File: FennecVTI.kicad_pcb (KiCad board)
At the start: 2 copper layers, 218 x 131.9 mm, 89 parts, among them J1 Expansion Connector, J2 Slot Select, J3 Conn_Coaxial, J4 MDA/CGA connector, J5 DB15_Female, J6 DIP14 Keyboard Connector, J7 User Connector, Q1 2N3906, U1 74LS191, U10 74LS574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

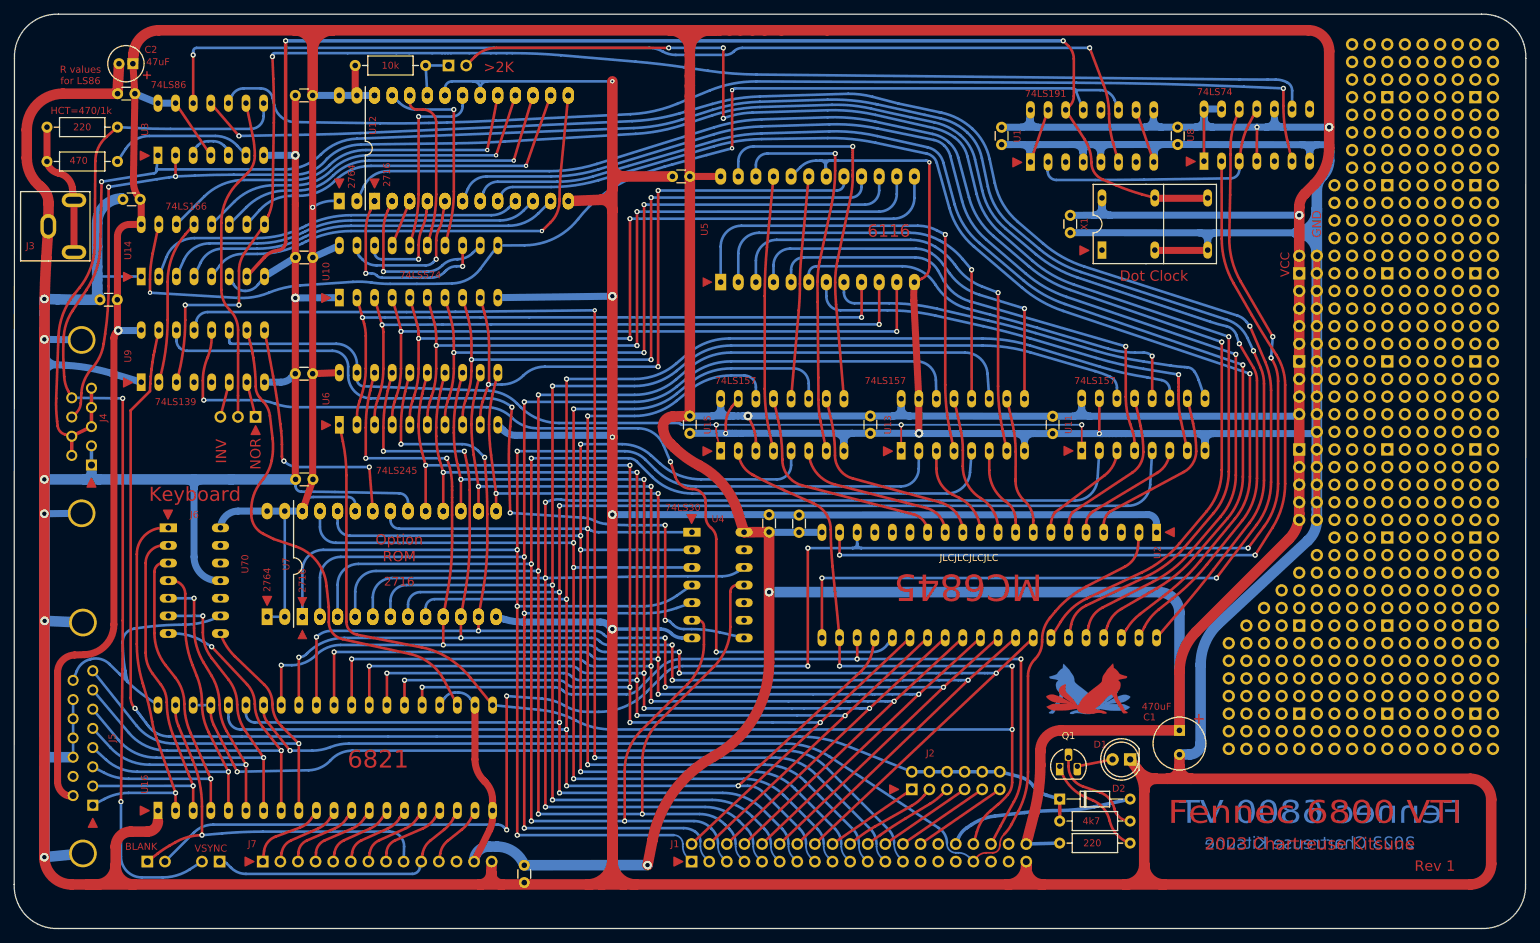
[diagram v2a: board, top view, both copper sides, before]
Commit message: Tweaked 2764 pinouts, cleanup DRC
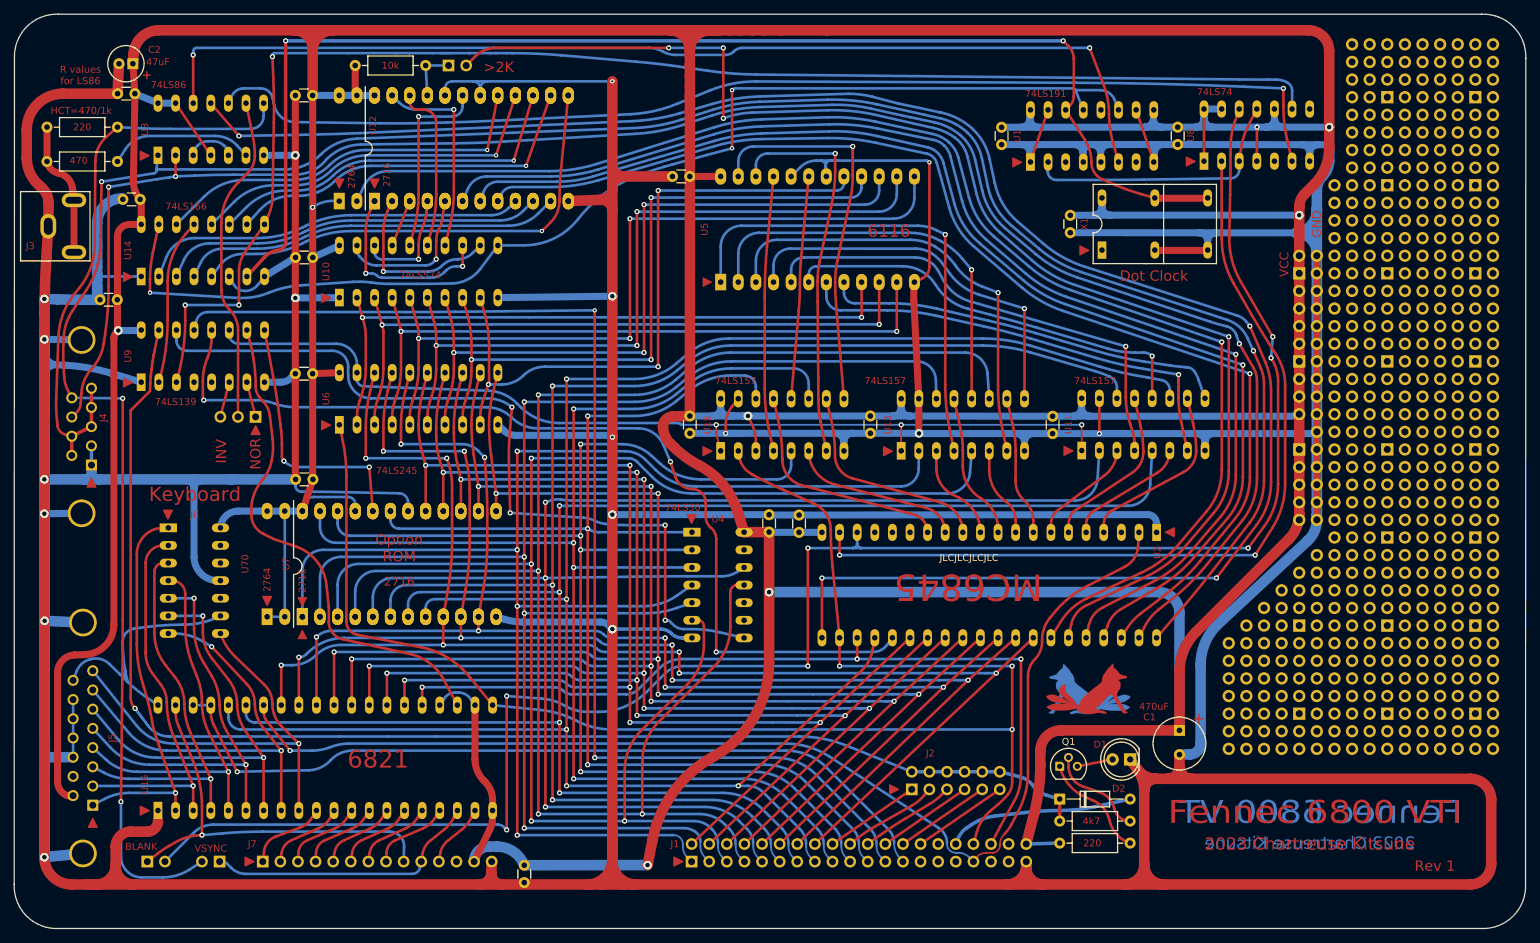
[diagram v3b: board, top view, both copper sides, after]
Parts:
- Q1: footprint Package_TO_SOT_THT:TO-92_HandSolder -> Package_TO_SOT_THT:TO-92
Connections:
- J4 pad 0: (no net) -> GND
- J5 pad 0: (no net) -> GND
- U120 pad 1: unconnected-(U120-VPP-Pad1) -> VCC
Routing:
- net /~{VRAMCS}: track 141.7 -> 141.2 mm
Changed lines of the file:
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@@
   (net 157 "unconnected-(U9A-O1-Pad5)")
   (net 158 "unconnected-(X1-NC-Pad1)")
-  (net 159 "unconnected-(U120-VPP-Pad1)")
   (footprint "Connector_PinHeader_2.54mm:PinHeader_1x14_P2.54mm_Vertical" (layer "F.Cu")
     (at 72.771 147.828 90)
@@
     (fp_arc (start 5.36 1.42) (mid 6.96 -0.18) (end 8.56 1.42)
       (stroke (width 0.1) (type solid)) (layer "F.Fab"))
-    (pad "0" thru_hole circle (at -18.04 1.42 270) (size 4 4) (drill 3.2) (layers "*.Cu" "*.Mask"))
-    (pad "0" thru_hole circle (at 6.96 1.42 270) (size 4 4) (drill 3.2) (layers "*.Cu" "*.Mask"))
+    (pad "0" thru_hole circle (at -18.04 1.42 270) (size 4 4) (drill 3.2) (layers "*.Cu" "*.Mask")
+      (net 2 "GND"))
+    (pad "0" thru_hole circle (at 6.96 1.42 270) (size 4 4) (drill 3.2) (layers "*.Cu" "*.Mask")
+      (net 2 "GND"))
     (pad "1" thru_hole rect (at 0 0 270) (size 1.6 1.6) (drill 1) (layers "*.Cu" "*.Mask")
       (net 2 "GND") (pinfunction "1") (pintype "passive"))
@@
     )
   )
-  (footprint "Package_TO_SOT_THT:TO-92_HandSolder" (layer "F.Cu")
+  (footprint "Package_TO_SOT_THT:TO-92" (layer "F.Cu")
     (at 187.706 134.091)
-    (descr "TO-92 leads molded, narrow, drill 0.75mm, handsoldering variant with enlarged pads (see NXP sot054_po.pdf)")
+    (descr "TO-92 leads molded, narrow, drill 0.75mm (see NXP sot054_po.pdf)")
     (tags "to-92 sc-43 sc-43a sot54 PA33 transistor")
     (property "Sheetfile" "FennecVTI.kicad_sch")
@@
     (property "ki_keywords" "PNP Transistor")
     (attr through_hole)
-    (fp_text reference "Q1" (at 1.27 -4.4) (layer "F.SilkS")
+    (fp_text reference "Q1" (at 1.27 -3.56) (layer "F.SilkS")
         (effects (font (size 1 1) (thickness 0.15)))
     )
@@
     (fp_line (start -0.53 1.85) (end 3.07 1.85)
       (stroke (width 0.12) (type solid)) (layer "F.SilkS"))
-    (fp_arc (start -0.541875 1.841741) (mid -1.247231 -0.581764) (end 0.45 -2.45)
+    (fp_arc (start -0.568478 1.838478) (mid -1.132087 -0.994977) (end 1.27 -2.6)
       (stroke (width 0.12) (type solid)) (layer "F.SilkS"))
-    (fp_arc (start 2.05 -2.45) (mid 3.769931 -0.601036) (end 3.078445 1.827684)
+    (fp_arc (start 1.27 -2.6) (mid 3.672087 -0.994977) (end 3.108478 1.838478)
       (stroke (width 0.12) (type solid)) (layer "F.SilkS"))
-    (fp_line (start -1.46 -3.05) (end -1.46 2.01)
+    (fp_line (start -1.46 -2.73) (end -1.46 2.01)
       (stroke (width 0.05) (type solid)) (layer "F.CrtYd"))
-    (fp_line (start -1.46 -3.05) (end 4 -3.05)
+    (fp_line (start -1.46 -2.73) (end 4 -2.73)
       (stroke (width 0.05) (type solid)) (layer "F.CrtYd"))
     (fp_line (start 4 2.01) (end -1.46 2.01)
       (stroke (width 0.05) (type solid)) (layer "F.CrtYd"))
-    (fp_line (start 4 2.01) (end 4 -3.05)
+    (fp_line (start 4 2.01) (end 4 -2.73)
       (stroke (width 0.05) (type solid)) (layer "F.CrtYd"))
     (fp_line (start -0.5 1.75) (end 3 1.75)
@@
     (fp_arc (start 1.27 -2.48) (mid 3.561221 -0.949055) (end 3.023625 1.753625)
       (stroke (width 0.1) (type solid)) (layer "F.Fab"))
-    (pad "1" thru_hole rect (at 0 0) (size 1.1 1.8) (drill 0.75 (offset 0 0.4)) (layers "*.Cu" "*.Mask")
+    (pad "1" thru_hole roundrect (at 0 0) (size 1.3 1.3) (drill 0.75) (layers "*.Cu" "*.Mask") (roundrect_rratio 0)
+      (chamfer_ratio 0.25) (chamfer top_right)
       (net 77 "Net-(Q1-E)") (pinfunction "E") (pintype "passive"))
-    (pad "2" thru_hole roundrect (at 1.27 -1.27) (size 1.1 1.8) (drill 0.75 (offset 0 -0.4)) (layers "*.Cu" "*.Mask") (roundrect_rratio 0.25)
+    (pad "2" thru_hole circle (at 1.27 -1.27) (size 1.3 1.3) (drill 0.75) (layers "*.Cu" "*.Mask")
       (net 79 "Net-(Q1-B)") (pinfunction "B") (pintype "input"))
-    (pad "3" thru_hole roundrect (at 2.54 0) (size 1.1 1.8) (drill 0.75 (offset 0 0.4)) (layers "*.Cu" "*.Mask") (roundrect_rratio 0.25)
+    (pad "3" thru_hole circle (at 2.54 0) (size 1.3 1.3) (drill 0.75) (layers "*.Cu" "*.Mask")
       (net 3 "Net-(D1-A)") (pinfunction "C") (pintype "passive"))
     (model "${KICAD6_3DMODEL_DIR}/Package_TO_SOT_THT.3dshapes/TO-92.wrl"
@@
         (effects (font (size 1 1) (thickness 0.15)))
     )
-    (fp_text value "470uF" (at -3.427349 3.302 180) (layer "F.Cu")
+    (fp_text value "470uF" (at -3.427349 3.683 180) (layer "F.Cu")
         (effects (font (size 1 1) (thickness 0.15)))
     )
@@
     (fp_arc (start 5.355 1.42) (mid 6.955 -0.18) (end 8.555 1.42)
       (stroke (width 0.1) (type solid)) (layer "F.Fab"))
-    (pad "0" thru_hole circle (at -26.345 1.42 270) (size 4 4) (drill 3.2) (layers "*.Cu" "*.Mask"))
-    (pad "0" thru_hole circle (at 6.955 1.42 270) (size 4 4) (drill 3.2) (layers "*.Cu" "*.Mask" "Eco2.User"))
+    (pad "0" thru_hole circle (at -26.345 1.42 270) (size 4 4) (drill 3.2) (layers "*.Cu" "*.Mask")
+      (net 2 "GND"))
+    (pad "0" thru_hole circle (at 6.955 1.42 270) (size 4 4) (drill 3.2) (layers "*.Cu" "*.Mask" "Eco2.User")
+      (net 2 "GND"))
     (pad "1" thru_hole rect (at 0 0 270) (size 1.6 1.6) (drill 1) (layers "*.Cu" "*.Mask")
       (net 48 "/KEYD0") (pinfunction "1") (pintype "passive"))
@@
       (stroke (width 0.1) (type solid)) (layer "F.Fab"))
     (pad "1" thru_hole rect (at 0 0 90) (size 2.4 1.6) (drill 0.8) (layers "*.Cu" "*.Mask")
-      (net 159 "unconnected-(U120-VPP-Pad1)") (pinfunction "VPP") (pintype "input"))
+      (net 1 "VCC") (pinfunction "VPP") (pintype "input"))
     (pad "2" thru_hole oval (at 0 2.54 90) (size 2.4 1.6) (drill 0.8) (layers "*.Cu" "*.Mask")
       (net 101 "/RA4") (pinfunction "A12") (pintype "input"))
@@
     (property "ki_keywords" "cap capacitor")
     (attr through_hole)
-    (fp_text reference "C2" (at -2.600887 2.032) (layer "F.Cu")
+    (fp_text reference "C2" (at -3.108887 2.032) (layer "F.Cu")
         (effects (font (size 1 1) (thickness 0.15)))
     )
@@
     (effects (font (size 1.5 1.5) (thickness 0.3)))
   )
-  (gr_text "VCC" (at 220.218 61.722 90) (layer "F.Cu")
+  (gr_text "VCC" (at 220.091 61.722 90) (layer "F.Cu")
     (effects (font (size 1.27 1.27) (thickness 0.2286)))
   )
@@
   (via (at 138.176 84.836) (size 0.762) (drill 0.381) (layers "F.Cu" "B.Cu") (net 129))
   (arc (start 138.332915 86.721306) (mid 138.215382 86.101057) (end 138.176 85.471) (width 0.254) (layer "F.Cu") (net 129))
-  (segment (start 86.36 76.322249) (end 86.36 76.662749) (width 0.381) (layer "B.Cu") (net 129))
-  (segment (start 86.36 77.91975) (end 86.36 77.7495) (width 0.381) (layer "B.Cu") (net 129))
   (segment (start 190.881 84.836) (end 164.846 84.836) (width 0.254) (layer "B.Cu") (net 129))
-  (segment (start 68.227526 73.152) (end 83.36 73.152) (width 0.381) (layer "B.Cu") (net 129))
+  (segment (start 86.36 78.282) (end 86.36 78.16125) (width 0.381) (layer "B.Cu") (net 129))
+  (segment (start 86.36 78.16125) (end 86.36 76.151999) (width 0.381) (layer "B.Cu") (net 129))
+  (segment (start 109.982 82.296) (end 109.417865 81.731865) (width 0.381) (layer "B.Cu") (net 129))
+  (segment (start 105.262465 79.923088) (end 87.325384 79.282478) (width 0.381) (layer "B.Cu") (net 129))
+  (segment (start 67.945 71.810481) (end 67.945 71.17) (width 0.381) (layer "B.Cu") (net 129))
   (segment (start 132.662394 84.582) (end 115.500892 84.582) (width 0.381) (layer "B.Cu") (net 129))
-  (segment (start 86.36 76.9815) (end 86.36 77.3655) (width 0.381) (layer "B.Cu") (net 129))
-  (segment (start 87.325384 79.282478) (end 105.262465 79.923088) (width 0.381) (layer "B.Cu") (net 129))
-  (segment (start 86.36 77.91975) (end 86.36 78.16125) (width 0.381) (layer "B.Cu") (net 129))
-  (segment (start 67.945 72.869473) (end 67.945 71.17) (width 0.381) (layer "B.Cu") (net 129))
-  (segment (start 86.36 76.322249) (end 86.36 76.151999) (width 0.381) (layer "B.Cu") (net 129))
-  (segment (start 109.417865 81.731865) (end 109.982 82.296) (width 0.381) (layer "B.Cu") (net 129))
-  (segment (start 86.36 78.16125) (end 86.36 78.282) (width 0.381) (layer "B.Cu") (net 129))
-  (segment (start 86.36 77.3655) (end 86.36 77.7495) (width 0.381) (layer "B.Cu") (net 129))
-  (segment (start 86.36 76.662749) (end 86.36 76.9815) (width 0.381) (layer "B.Cu") (net 129))
+  (segment (start 83.36 73.152) (end 69.286519 73.152) (width 0.381) (layer "B.Cu") (net 129))
   (segment (start 164.846 84.836) (end 138.176 84.836) (width 0.254) (layer "B.Cu") (net 129))
   (segment (start 133.275605 84.836) (end 138.176 84.836) (width 0.254) (layer "B.Cu") (net 129))
+  (arc (start 87.325384 79.282478) (mid 86.640697 78.977148) (end 86.36 78.282) (width 0.381) (layer "B.Cu") (net 129))
   (arc (start 115.500892 84.582) (mid 112.514089 83.987887) (end 109.982 82.296) (width 0.381) (layer "B.Cu") (net 129))
+  (arc (start 132.969 84.709) (mid 132.828328 84.615006) (end 132.662394 84.582) (width 0.381) (layer "B.Cu") (net 129))
+  (arc (start 67.945 71.810481) (mid 68.337922 72.759078) (end 69.286519 73.152) (width 0.381) (layer "B.Cu") (net 129))
   (arc (start 86.36 76.151999) (mid 85.48132 74.030679) (end 83.36 73.152) (width 0.381) (layer "B.Cu") (net 129))
-  (arc (start 67.945 72.869473) (mid 67.966506 72.977591) (end 68.02775 73.06925) (width 0.381) (layer "B.Cu") (net 129))
-  (arc (start 132.662394 84.582) (mid 132.828328 84.615006) (end 132.969 84.709) (width 0.381) (layer "B.Cu") (net 129))
-  (arc (start 87.325384 79.282478) (mid 86.640697 78.977148) (end 86.36 78.282) (width 0.381) (layer "B.Cu") (net 129))
   (arc (start 133.275605 84.836) (mid 133.109671 84.802993) (end 132.969 84.709) (width 0.381) (layer "B.Cu") (net 129))
   (arc (start 109.417865 81.731865) (mid 107.511683 80.43344) (end 105.262465 79.923088) (width 0.381) (layer "B.Cu") (net 129))
-  (arc (start 68.227526 73.152) (mid 68.119408 73.130493) (end 68.02775 73.06925) (width 0.381) (layer "B.Cu") (net 129))
   (segment (start 88.138 90.932) (end 88.646 97.287) (width 0.381) (layer "F.Cu") (net 130))
   (segment (start 75.309865 84.740811) (end 75.423596 85.71147) (width 0.381) (layer "F.Cu") (net 130))

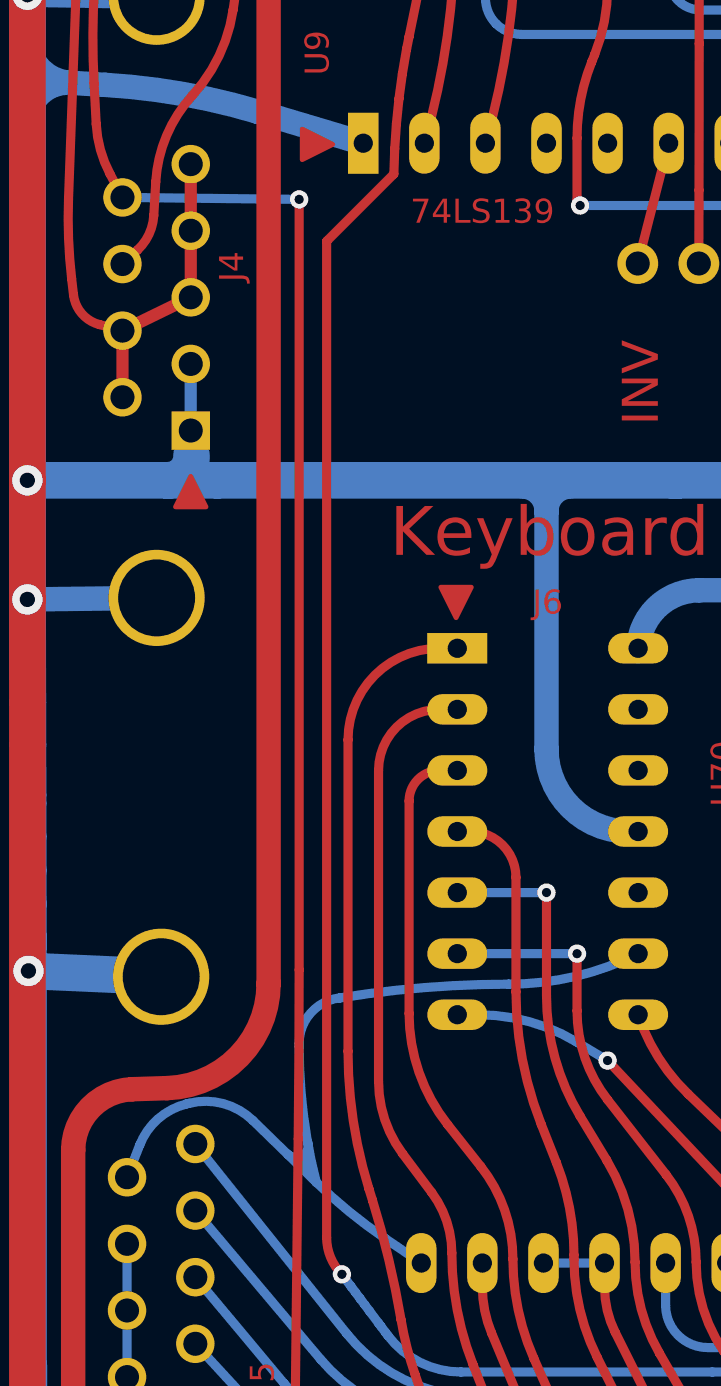
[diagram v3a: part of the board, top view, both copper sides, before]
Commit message: Added Teardrops
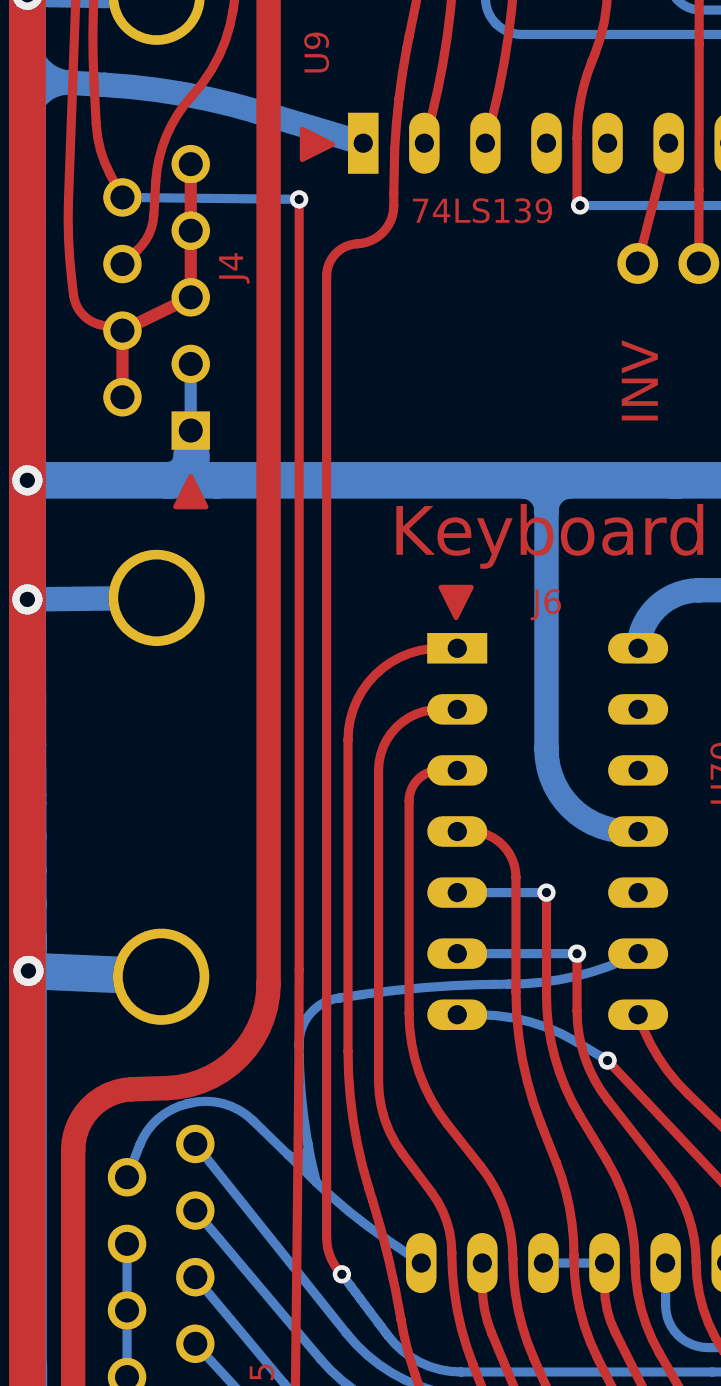
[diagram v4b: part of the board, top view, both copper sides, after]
